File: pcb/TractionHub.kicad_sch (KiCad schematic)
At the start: 0 parts

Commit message: pcb: add regulators and stm32
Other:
- added sheet microcontroller (microcontroller.kicad_sch)
- added sheet power (power.kicad_sch)
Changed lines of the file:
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@@
 		(company "ProMez - David Mezler")
+	)
+	(sheet
+		(at 64.77 81.28)
+		(size 38.1 25.4)
+		(fields_autoplaced yes)
+		(stroke
+			(width 0.1524)
+			(type solid)
+		)
+		(fill
+			(color 0 0 0 0.0000)
+		)
+		(property "Sheetname" "power"
+			(at 64.77 80.5684 0)
+			(effects
+				(font
+					(size 1.27 1.27)
+				)
+				(justify left bottom)
+			)
+		)
+		(property "Sheetfile" "power.kicad_sch"
+			(at 64.77 107.2646 0)
+			(effects
+				(font
+					(size 1.27 1.27)
+				)
+				(justify left top)
+			)
+		)
+		(pin "VCC_SENSE" output
+			(at 102.87 93.98 0)
+			(effects
+				(font
+					(size 1.27 1.27)
+				)
+				(justify right)
+			)
+		)
+		(instances
+			(project "TractionHub"
+				(path "/c6712b71-1d4c-4b1c-822a-6fd97117379c"
+					(page "2")
+				)
+			)
+		)
+	)
+	(sheet
+		(at 121.92 81.28)
+		(size 38.1 25.4)
+		(fields_autoplaced yes)
+		(stroke
+			(width 0.1524)
+			(type solid)
+		)
+		(fill
+			(color 0 0 0 0.0000)
+		)
+		(property "Sheetname" "microcontroller"
+			(at 121.92 80.5684 0)
+			(effects
+				(font
+					(size 1.27 1.27)
+				)
+				(justify left bottom)
+			)
+		)
+		(property "Sheetfile" "microcontroller.kicad_sch"
+			(at 121.92 107.2646 0)
+			(effects
+				(font
+					(size 1.27 1.27)
+				)
+				(justify left top)
+			)
+		)
+		(instances
+			(project "TractionHub"
+				(path "/c6712b71-1d4c-4b1c-822a-6fd97117379c"
+					(page "3")
+				)
+			)
+		)
 	)
 	(sheet_instances

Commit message: pcb: wip
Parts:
- added J3: MAIN_PWR_CON, Connector_AMASS:AMASS_XT60-M_1x02_P7.20mm_Vertical, symbol Connector_Generic:Conn_01x02
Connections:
- new net power/+VDC: J3.1 (Pin_1)
- new net power/PWR_GND: J3.2 (Pin_2)
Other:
- sheet power ports: added +VDC, PWR_GND; removed none
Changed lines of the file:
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@@
 		(company "ProMez - David Mezler")
+	)
+	(wire
+		(pts
+			(xy 57.15 92.71) (xy 64.77 92.71)
+		)
+		(stroke
+			(width 0)
+			(type default)
+		)
+	)
+	(wire
+		(pts
+			(xy 57.15 95.25) (xy 64.77 95.25)
+		)
+		(stroke
+			(width 0)
+			(type default)
+		)
+	)
+	(symbol
+		(lib_id "Connector_Generic:Conn_01x02")
+		(at 52.07 92.71 0)
+		(mirror y)
+		(unit 1)
+		(exclude_from_sim no)
+		(in_bom yes)
+		(on_board yes)
+		(dnp no)
+		(property "Reference" "J3"
+			(at 52.07 87.122 0)
+			(effects
+				(font
+					(size 1.27 1.27)
+				)
+			)
+		)
+		(property "Value" "MAIN_PWR_CON"
+			(at 52.324 89.662 0)
+			(effects
+				(font
+					(size 1.27 1.27)
+				)
+			)
+		)
+		(property "Footprint" "Connector_AMASS:AMASS_XT60-M_1x02_P7.20mm_Vertical"
+			(at 52.07 92.71 0)
+			(effects
+				(font
+					(size 1.27 1.27)
+				)
+				(hide yes)
+			)
+		)
+		(property "Datasheet" "https://www.tme.eu/Document/ceb306d6300f4d2860483975b79af125/XT60UPB-M.pdf"
+			(at 52.07 92.71 0)
+			(effects
+				(font
+					(size 1.27 1.27)
+				)
+				(hide yes)
+			)
+		)
+		(property "Description" "Generic connector, single row, 01x02, script generated (kicad-library-utils/schlib/autogen/connector/)"
+			(at 52.07 92.71 0)
+			(effects
+				(font
+					(size 1.27 1.27)
+				)
+				(hide yes)
+			)
+		)
+		(pin "2"
+		)
+		(pin "1"
+		)
+		(instances
+			(project "TractionHub"
+				(path "/c6712b71-1d4c-4b1c-822a-6fd97117379c"
+					(reference "J3")
+					(unit 1)
+				)
+			)
+		)
 	)
 	(sheet
@@
 		)
 		(pin "VCC_SENSE" output
-			(at 102.87 93.98 0)
+			(at 102.87 87.63 0)
 			(effects
 				(font
@@
 				)
 				(justify right)
+			)
+		)
+		(pin "PWR_GND" input
+			(at 64.77 95.25 180)
+			(effects
+				(font
+					(size 1.27 1.27)
+				)
+				(justify left)
+			)
+		)
+		(pin "+VDC" input
+			(at 64.77 92.71 180)
+			(effects
+				(font
+					(size 1.27 1.27)
+				)
+				(justify left)
 			)
 		)
@@
 	)
 	(sheet
-		(at 121.92 81.28)
+		(at 161.29 86.36)
 		(size 38.1 25.4)
 		(fields_autoplaced yes)
@@
 		)
 		(property "Sheetname" "microcontroller"
-			(at 121.92 80.5684 0)
+			(at 161.29 85.6484 0)
 			(effects
 				(font
@@
 		)
 		(property "Sheetfile" "microcontroller.kicad_sch"
-			(at 121.92 107.2646 0)
+			(at 161.29 112.3446 0)
 			(effects
 				(font

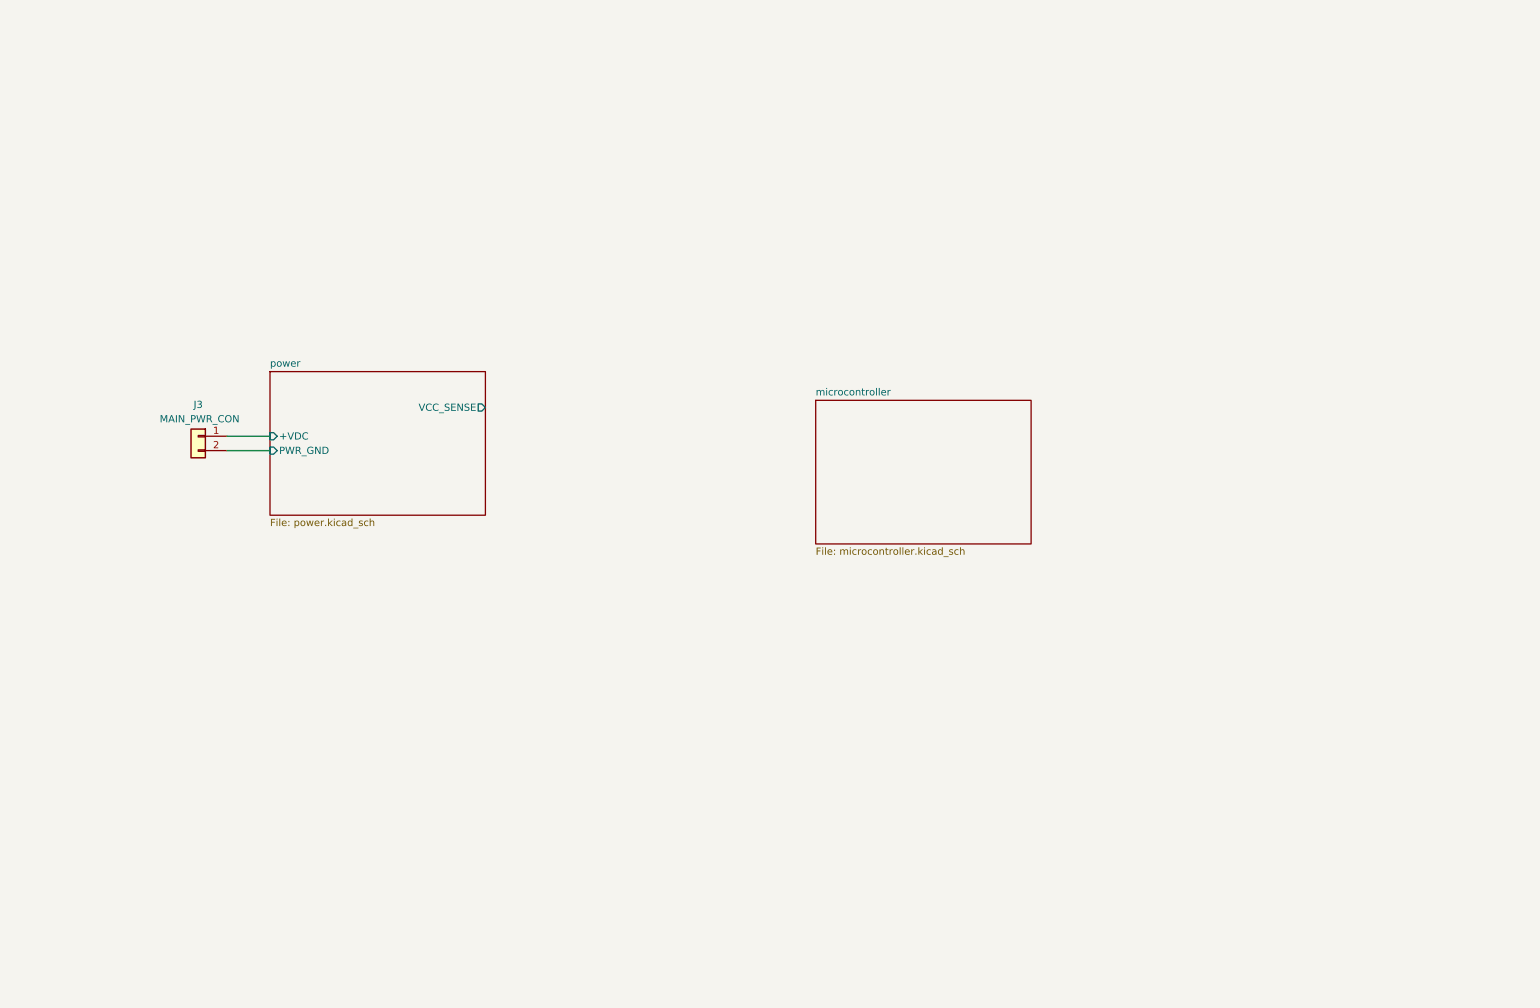
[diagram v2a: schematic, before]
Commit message: pcb: first version schematic
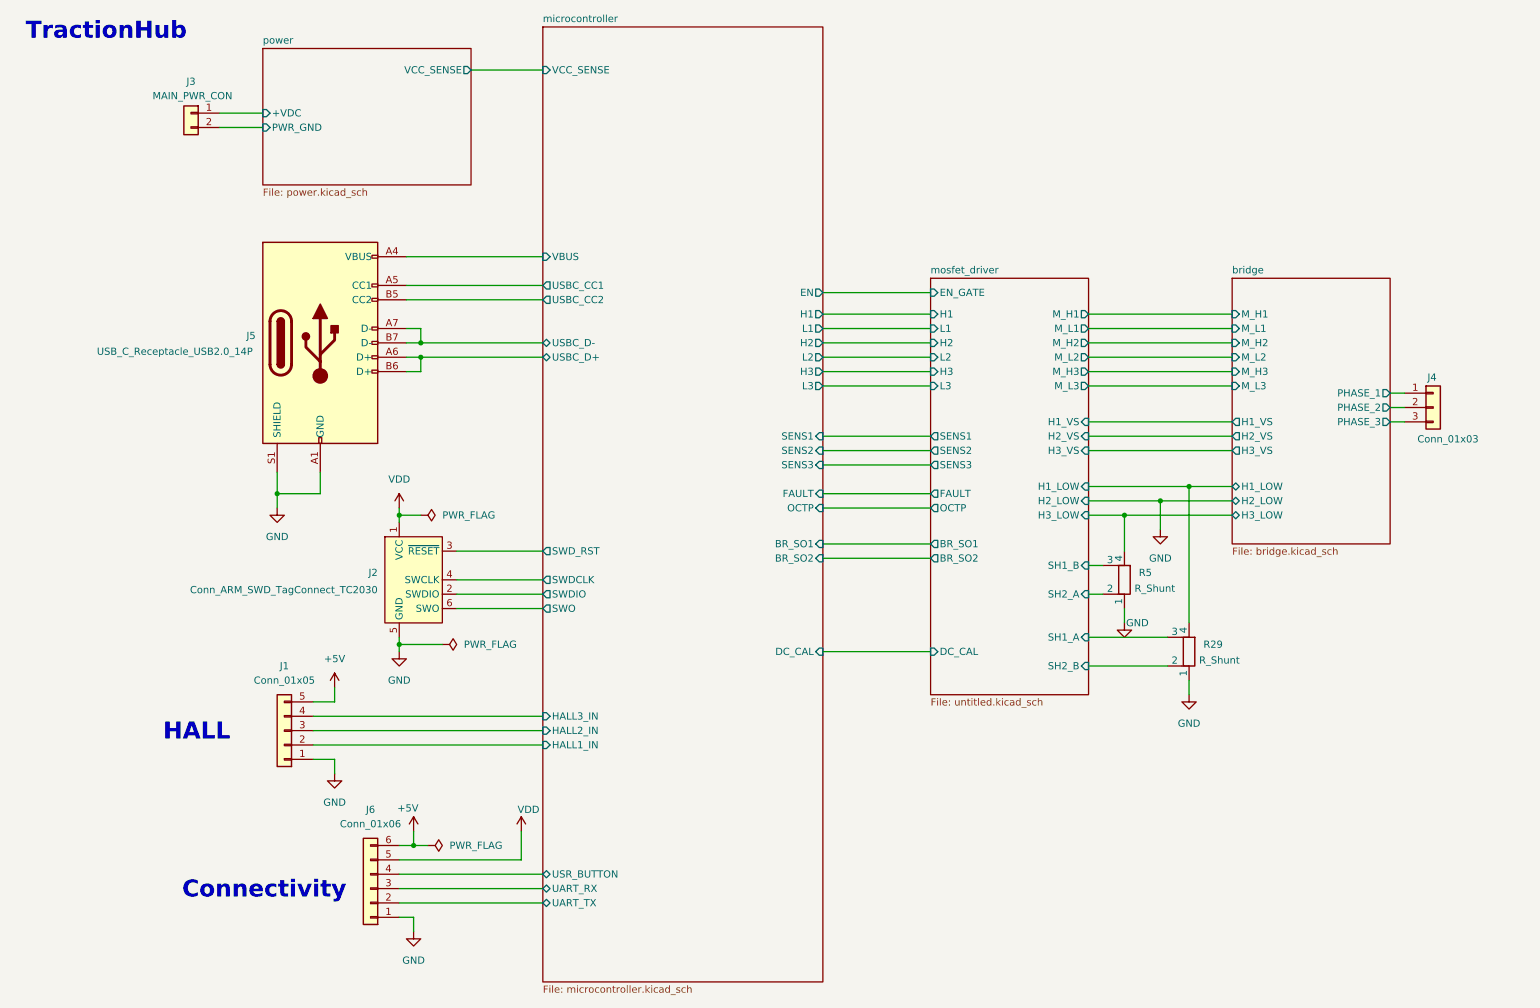
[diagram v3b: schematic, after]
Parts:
- added J1: Conn_01x05, Connector_JST:JST_EH_B5B-EH-A_1x05_P2.50mm_Vertical, symbol Connector_Generic:Conn_01x05
- added J2: Conn_ARM_SWD_TagConnect_TC2030, Connector:Tag-Connect_TC2030-IDC-FP_2x03_P1.27mm_Vertical, symbol Connector:Conn_ARM_SWD_TagConnect_TC2030
- added J4: Conn_01x03, tractions_symbols:cooler, symbol Connector_Generic:Conn_01x03
- added J5: USB_C_Receptacle_USB2.0_14P, Connector_USB:USB_C_Receptacle_GCT_USB4105-xx-A_16P_TopMnt_Horizontal, symbol Connector:USB_C_Receptacle_USB2.0_14P
- added J6: Conn_01x06, Connector_JST:JST_EH_B6B-EH-A_1x06_P2.50mm_Vertical, symbol Connector_Generic:Conn_01x06
- added R29, R5: R_Shunt, tractions_symbols:besser, symbol Device:R_Shunt
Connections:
- new net +5V: J1.5 (Pin_5), J6.6 (Pin_6)
- new net GND: J1.1 (Pin_1), J2.5 (GND), J5.A1 (GND), J5.A12 (GND), J5.B1 (GND), J5.B12 (GND), J5.S1 (SHIELD), J6.1 (Pin_1), R29.1, R5.1
- new net VDD: J2.1 (VCC), J6.5 (Pin_5)
- new net bridge/H1_LOW: R29.4
- new net bridge/H3_LOW: R5.4
- new net bridge/PHASE_1: J4.1 (Pin_1)
- new net bridge/PHASE_2: J4.2 (Pin_2)
- new net bridge/PHASE_3: J4.3 (Pin_3)
- new net microcontroller/HALL1_IN: J1.2 (Pin_2)
- new net microcontroller/HALL2_IN: J1.3 (Pin_3)
- new net microcontroller/HALL3_IN: J1.4 (Pin_4)
- new net microcontroller/SWDCLK: J2.4 (SWCLK)
- new net microcontroller/SWDIO: J2.2 (SWDIO)
- new net microcontroller/SWD_RST: J2.3 (~{RESET})
- new net microcontroller/SWO: J2.6 (SWO)
- new net microcontroller/UART_RX: J6.3 (Pin_3)
- new net microcontroller/UART_TX: J6.2 (Pin_2)
- new net microcontroller/USBC_CC1: J5.A5 (CC1)
- new net microcontroller/USBC_CC2: J5.B5 (CC2)
- new net microcontroller/USBC_D+: J5.A6 (D+), J5.B6 (D+)
- new net microcontroller/USBC_D-: J5.A7 (D-), J5.B7 (D-)
- new net microcontroller/USR_BUTTON: J6.4 (Pin_4)
- new net microcontroller/VBUS: J5.A4 (VBUS), J5.A9 (VBUS), J5.B4 (VBUS), J5.B9 (VBUS)
- new net mosfet_driver/SH1_A: R29.3
- new net mosfet_driver/SH1_B: R5.3
- new net mosfet_driver/SH2_A: R5.2
- new net mosfet_driver/SH2_B: R29.2
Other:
- added sheet bridge (bridge.kicad_sch)
- added sheet mosfet_driver (untitled.kicad_sch)
- sheet microcontroller ports: added BR_SO1, BR_SO2, DC_CAL, EN, FAULT, H1, H2, H3, HALL1_IN, HALL2_IN, HALL3_IN, L1, L2, L3, OCTP, SENS1, SENS2, SENS3, SWDCLK, SWDIO, SWD_RST, SWO, UART_RX, UART_TX, USBC_CC1, USBC_CC2, USBC_D+, USBC_D-, USR_BUTTON, VBUS, VCC_SENSE; removed none
- note added: "Connectivity"
- note added: "HALL"
- note added: "TractionHub"
- moved on the sheet: J3

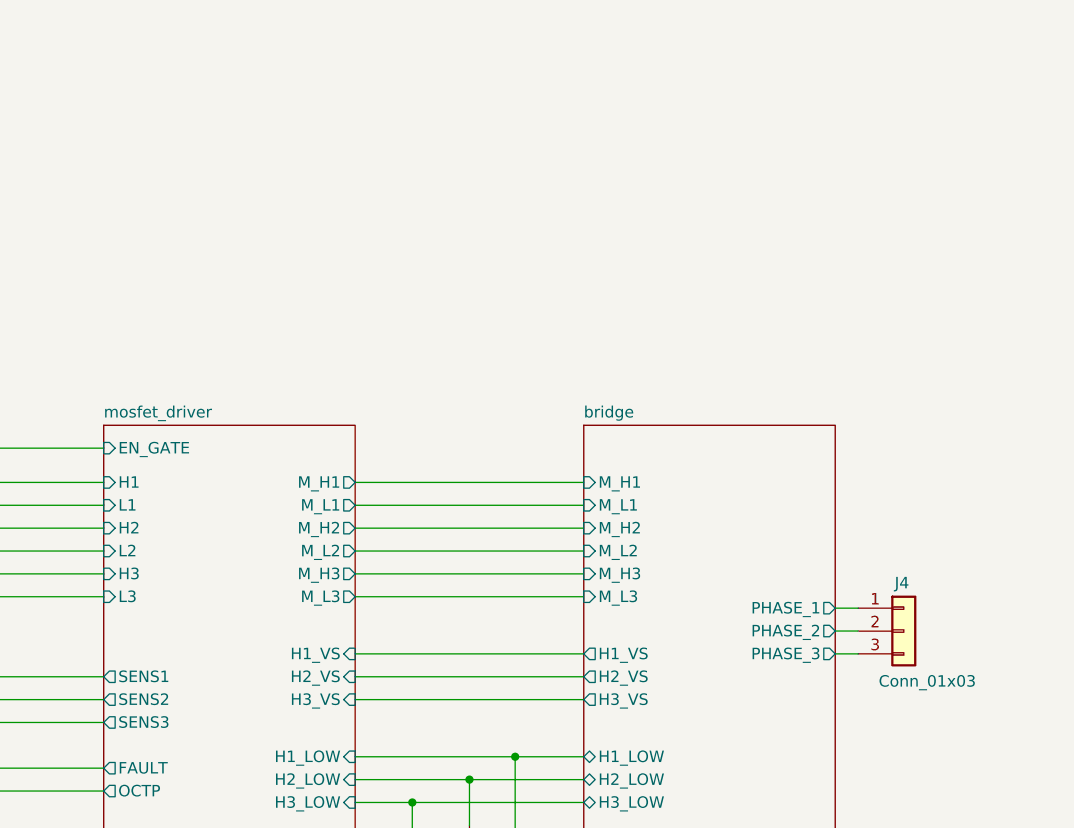
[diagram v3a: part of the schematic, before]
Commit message: pcb: outlines ready
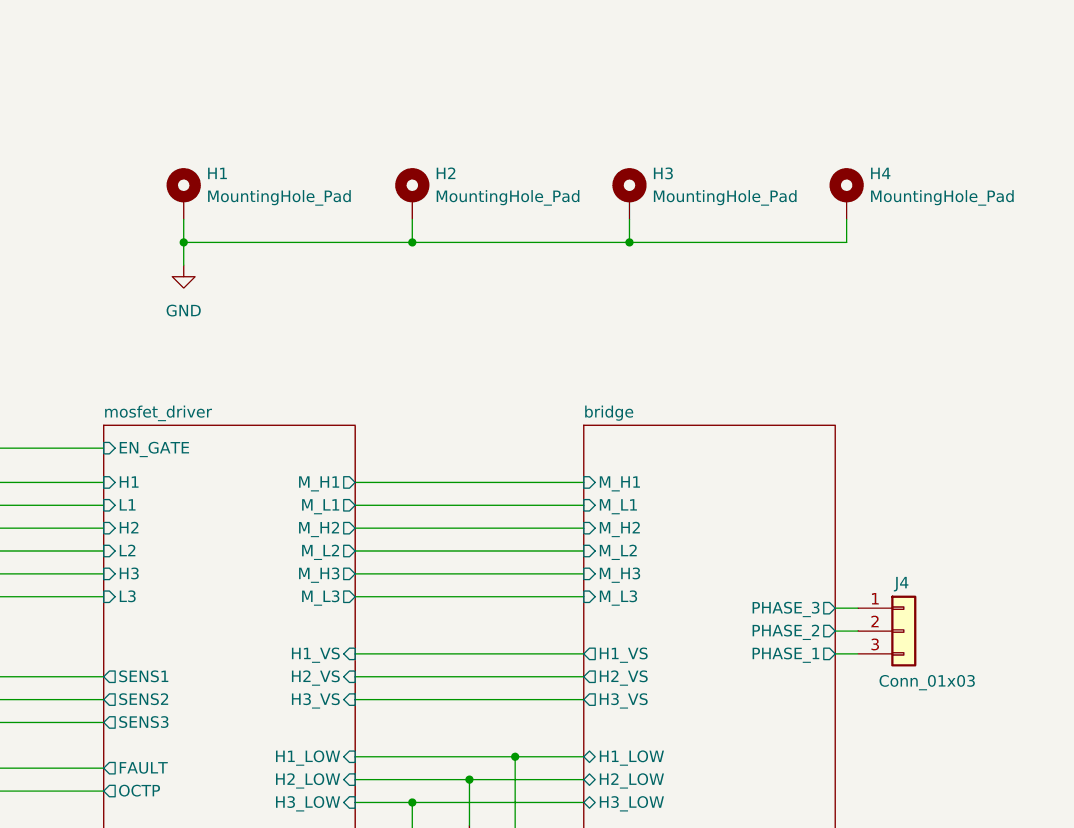
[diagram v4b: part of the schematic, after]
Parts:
- added H1, H2, H3, H4: MountingHole_Pad, MountingHole:MountingHole_4.3mm_M4_Pad_Via, symbol Mechanical:MountingHole_Pad
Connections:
- net GND: now also H1.1, H2.1, H3.1, H4.1
- net bridge/PHASE_1: now also J4.3 (Pin_3); no longer J4.1 (Pin_1)
- net bridge/PHASE_3: now also J4.1 (Pin_1); no longer J4.3 (Pin_3)

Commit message: pcb: layout gate driver
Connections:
- net mosfet_driver/SH1_A: now also R5.3; no longer R29.3
- net mosfet_driver/SH1_B: now also R5.2; no longer R5.3
- net mosfet_driver/SH2_A: now also R29.3; no longer R5.2
